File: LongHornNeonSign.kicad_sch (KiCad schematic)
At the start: 19 parts, among them Q1 IRLZ44N, Q2 IRLZ44N, Q3 IRLZ44N

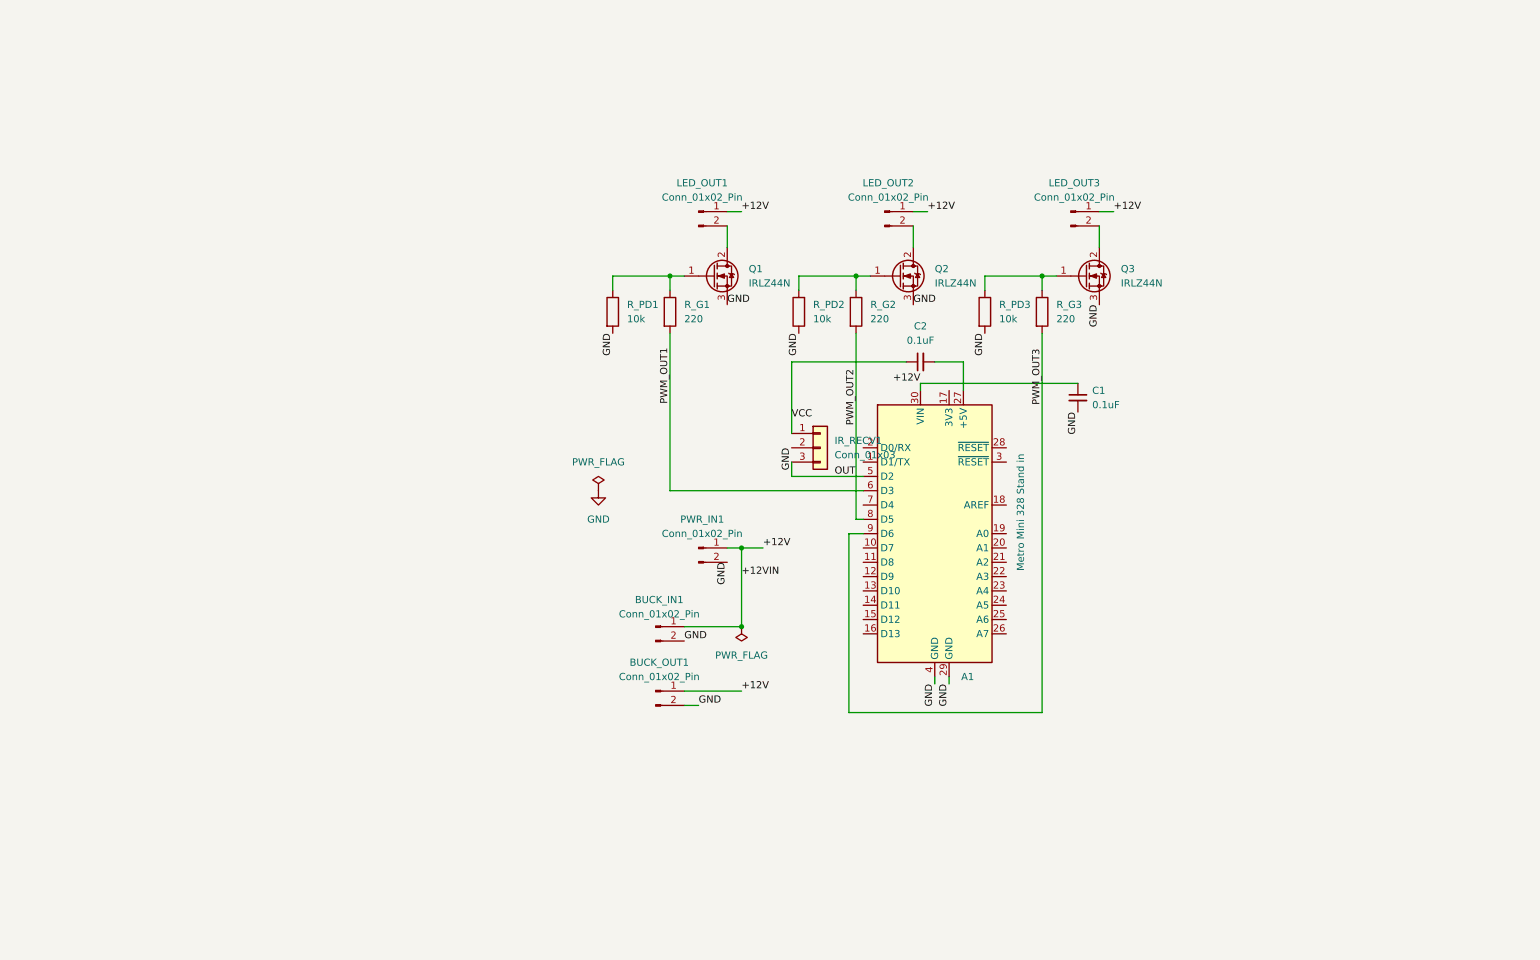
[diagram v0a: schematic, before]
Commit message: Fixed schematic
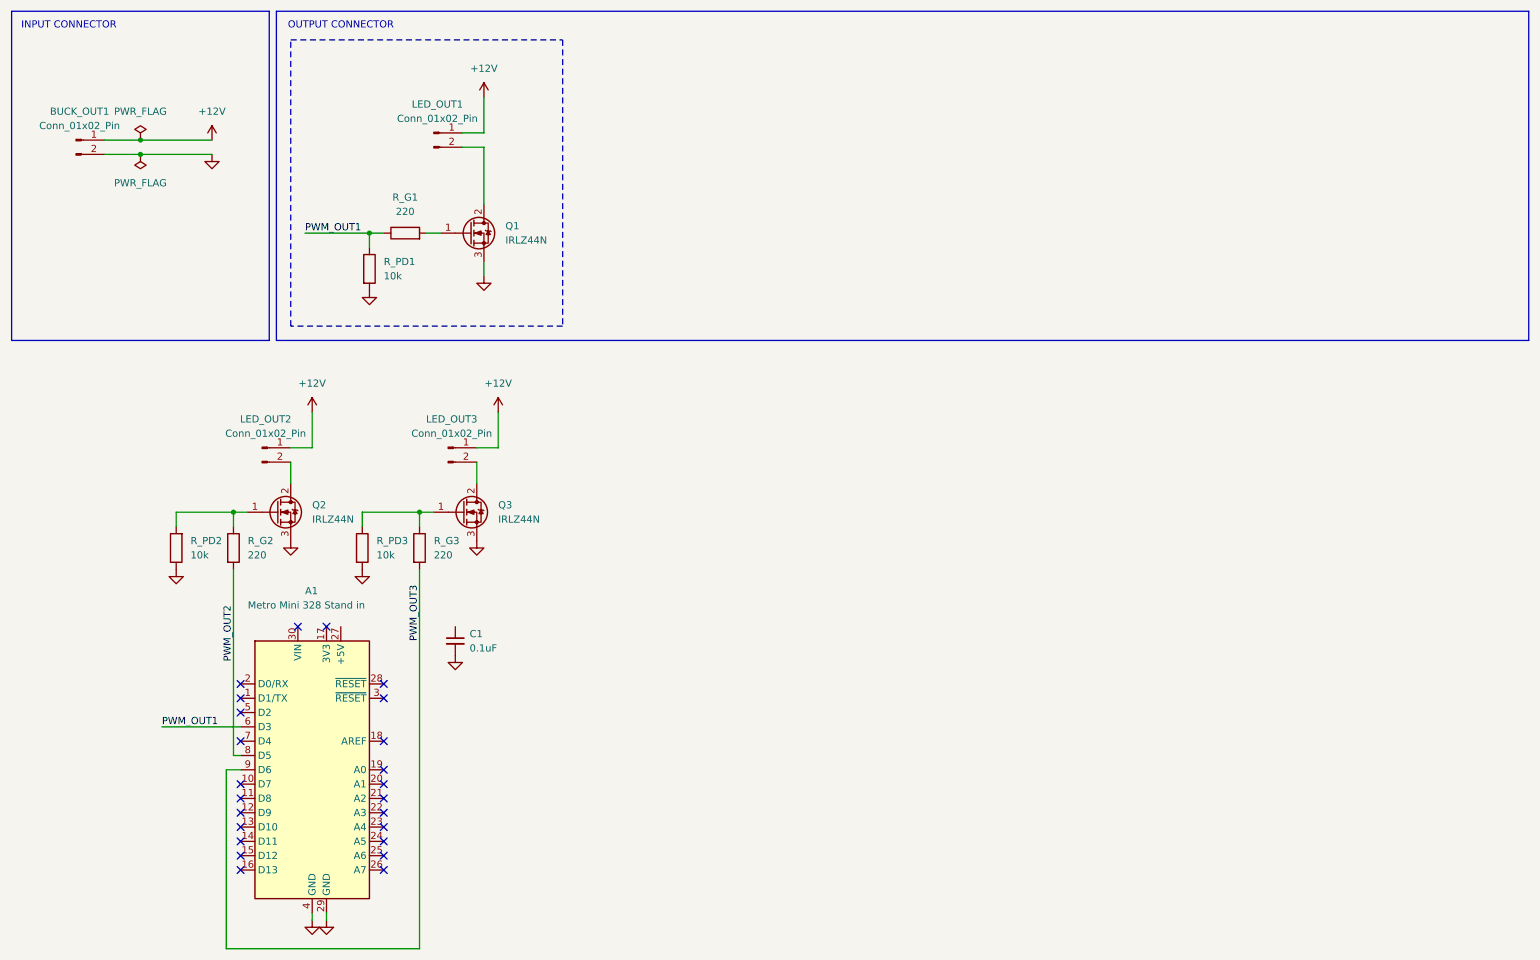
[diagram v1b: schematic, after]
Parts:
- removed BUCK_IN1, PWR_IN1: Conn_01x02_Pin, Connector_PinHeader_2.54mm:PinHeader_1x02_P2.54mm_Vertical, symbol Connector:Conn_01x02_Pin
- removed C2: 0.1uF, Capacitor_SMD:C_0805_2012Metric, symbol Device:C_Small
- removed IR_RECV1: Conn_01x03, Connector_PinHeader_2.54mm:PinHeader_1x03_P2.54mm_Vertical, symbol Connector_Generic:Conn_01x03
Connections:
- net PWM_OUT1: now also R_G1.1, R_PD1.1; no longer R_G1.2
- net +12V  renamed +12V
- net +12V: no longer A1.30 (VIN), C1.1
- net OUT: no longer names the net of A1.5 (D2)
- new net: Q1.1 (G), R_G1.2
- no-connect marks 0 -> 24
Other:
- note added: "INPUT CONNECTOR"
- note added: "OUTPUT CONNECTOR"
- moved on the sheet: A1, BUCK_OUT1, C1, LED_OUT1, LED_OUT2, LED_OUT3, Q1, Q2, Q3, R_G1, R_G2, R_G3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

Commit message: update sch
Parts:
- added BUCK_IN1, BUCK_OUT1: Conn_01x02_Pin, Connector_PinHeader_2.54mm:PinHeader_1x02_P2.54mm_Vertical, symbol Connector:Conn_01x02_Pin
- added C_DEBOUNCE1, C_DEBOUNCE2, C_DEBOUNCE3: 0.1uF, Capacitor_SMD:C_0805_2012Metric, symbol Device:C_Small
- added LED_12V1, LED_5V1: LED, LED_THT:LED_D5.0mm, symbol Device:LED
- added LED_OUT4: Conn_01x02_Pin, LED_THT:LED_D5.0mm, symbol Connector:Conn_01x02_Pin
- added Q4: IRLZ44N, Package_TO_SOT_THT:TO-220-3_Vertical, symbol Transistor_FET:IRLZ44N
- added R1: 1kΩ, Resistor_THT:R_Axial_DIN0207_L6.3mm_D2.5mm_P7.62mm, symbol Device:R
- added R2: 470Ω, Resistor_THT:R_Axial_DIN0207_L6.3mm_D2.5mm_P7.62mm, symbol Device:R
- added R_G4: 220, Resistor_THT:R_Axial_DIN0207_L6.3mm_D2.5mm_P7.62mm_Horizontal, symbol Device:R
- added R_PD4, R_PD5, R_PD6, R_PD7: 10kΩ, Resistor_THT:R_Axial_DIN0207_L6.3mm_D2.5mm_P7.62mm_Horizontal, symbol Device:R
- added SW1, SW2, SW3: SW_Push, Button_Switch_THT:SW_PUSH_6mm, symbol Switch:SW_Push
- A1: value Metro Mini 328 Stand in -> Arduino Nano
- R_PD1, R_PD2, R_PD3: value 10k -> 10kΩ
- renumbered BUCK_OUT1 to PWR_IN1
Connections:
- net +12V: now also BUCK_IN1.1 (Pin_1), LED_OUT4.1 (Pin_1), R1.1
- net GND: now also R_PD2.2, BUCK_IN1.2 (Pin_2), BUCK_OUT1.2 (Pin_2), C_DEBOUNCE1.1, C_DEBOUNCE2.1, C_DEBOUNCE3.1, LED_12V1.2 (A), LED_5V1.2 (A), Q4.3 (S), R_PD4.2, R_PD5.2, R_PD6.2, R_PD7.2; no longer R_PD2.1
- net PWM_OUT2: now also R_G2.1, R_PD2.1; no longer R_G2.2
- net PWM_OUT3: now also R_G3.1, R_PD3.1; no longer R_G3.2
- net at C1.1: now also A1.27 (+5V)
- net BTN_DOWN: now reaches A1.10 (D7)
- net BTN_DOWN: now also C_DEBOUNCE3.2, R_PD6.1, SW3.2
- net PWM_OUT4: now reaches A1.11 (D8)
- net PWM_OUT4: now also R_G4.1, R_PD7.1
- net BTN_TOGGLE: now reaches A1.5 (D2)
- net BTN_TOGGLE: now also C_DEBOUNCE1.2, R_PD4.1, SW1.2
- net BTN_UP: now reaches A1.7 (D4)
- net BTN_UP: now also C_DEBOUNCE2.2, R_PD5.1, SW2.2
- new net: LED_5V1.1 (K), R2.2
- new net: LED_OUT4.2 (Pin_2), Q4.2 (D)
- new net: Q3.1 (G), R_G3.2
- new net: LED_12V1.1 (K), R1.2
- new net: Q4.1 (G), R_G4.2
- new net: Q2.1 (G), R_G2.2
- new net +5V: BUCK_OUT1.1 (Pin_1), R2.1, SW1.1, SW2.1, SW3.1
- no-connect marks 24 -> 20
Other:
- note added: "BUCK CONVERTER"
- note added: "BUTTONS"
- note added: "DEBUG LEDS"
- note added: "OUTPUT CONNECTOR (1)"
- note added: "OUTPUT CONNECTOR (2)"
- moved on the sheet: A1, C1, LED_OUT1, PWR_IN1, Q1, R_G1, R_PD1

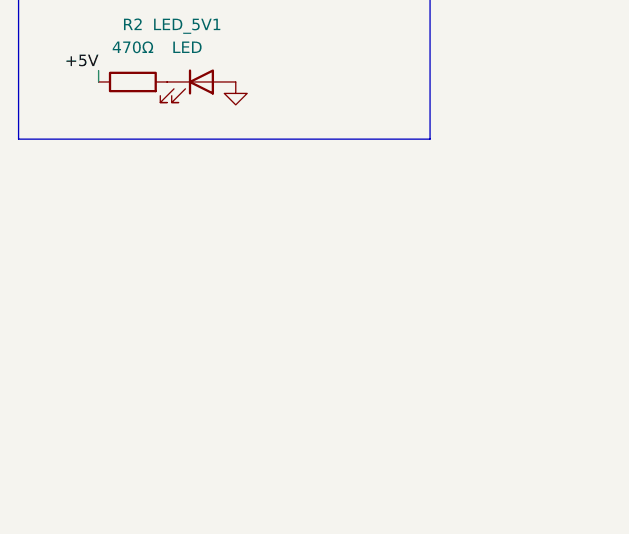
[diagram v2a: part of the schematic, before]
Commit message: Added testpoint example
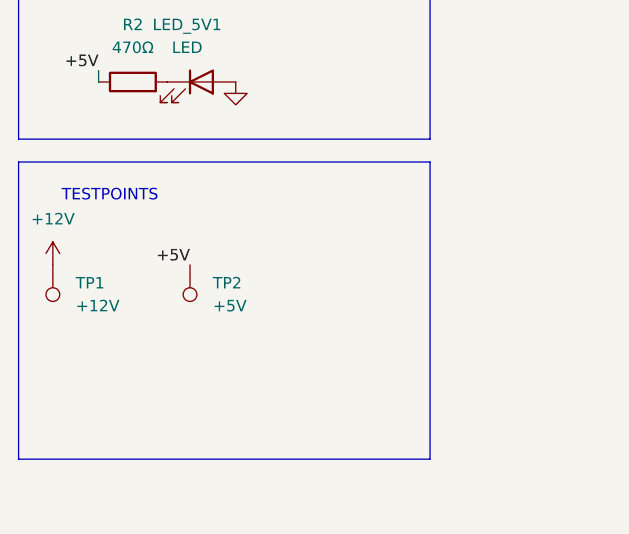
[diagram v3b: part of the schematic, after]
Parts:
- added TP1: +12V, Connector_PinHeader_2.54mm:PinHeader_1x01_P2.54mm_Vertical, symbol Connector:TestPoint
- added TP2: +5V, Connector_PinHeader_2.54mm:PinHeader_1x01_P2.54mm_Vertical, symbol Connector:TestPoint
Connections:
- net +12V: now also TP1.1
- net +5V: now also TP2.1
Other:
- note added: "TESTPOINTS"
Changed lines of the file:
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@@
+	)
+	(rectangle
+		(start 13.97 110.49)
+		(end 59.69 143.51)
+		(stroke
+			(width 0)
+			(type default)
+		)
+		(fill
+			(type none)
+		)
 	)
 	(rectangle
@@
 		(fill
 			(type none)
+		)
+	)
+	(text "TESTPOINTS\n"
+		(exclude_from_sim no)
+		(at 24.13 114.3 0)
+		(effects
+			(font
+				(size 1.27 1.27)
+			)
 		)
 	)
@@
 	(label "BTN_TOGGLE"
 		(at 100.33 110.49 180)
+		(effects
+			(font
+				(size 1.27 1.27)
+			)
+			(justify right bottom)
+		)
+	)
+	(label "+5V"
+		(at 33.02 121.92 180)
 		(effects
 			(font
@@
 	)
 	(symbol
+		(lib_id "Connector:TestPoint")
+		(at 33.02 121.92 180)
+		(unit 1)
+		(exclude_from_sim no)
+		(in_bom yes)
+		(on_board yes)
+		(dnp no)
+		(fields_autoplaced yes)
+		(property "Reference" "TP2"
+			(at 35.56 123.9519 0)
+			(effects
+				(font
+					(size 1.27 1.27)
+				)
+				(justify right)
+			)
+		)
+		(property "Value" "+5V"
+			(at 35.56 126.4919 0)
+			(effects
+				(font
+					(size 1.27 1.27)
+				)
+				(justify right)
+			)
+		)
+		(property "Footprint" "Connector_PinHeader_2.54mm:PinHeader_1x01_P2.54mm_Vertical"
+			(at 27.94 121.92 0)
+			(effects
+				(font
+					(size 1.27 1.27)
+				)
+				(hide yes)
+			)
+		)
+		(property "Datasheet" "~"
+			(at 27.94 121.92 0)
+			(effects
+				(font
+					(size 1.27 1.27)
+				)
+				(hide yes)
+			)
+		)
+		(property "Description" "test point"
+			(at 33.02 121.92 0)
+			(effects
+				(font
+					(size 1.27 1.27)
+				)
+				(hide yes)
+			)
+		)
+		(pin "1"
+		)
+		(instances
+			(project "LongHornNeonSign"
+				(path "/f5140a03-2151-4444-9841-b9751d5275da"
+					(reference "TP2")
+					(unit 1)
+				)
+			)
+		)
+	)
+	(symbol
 		(lib_id "power:GND")
 		(at 101.6 60.96 0)
@@
 	)
 	(symbol
+		(lib_id "power:+12V")
+		(at 17.78 121.92 0)
+		(unit 1)
+		(exclude_from_sim no)
+		(in_bom yes)
+		(on_board yes)
+		(dnp no)
+		(fields_autoplaced yes)
+		(property "Reference" "#PWR030"
+			(at 17.78 125.73 0)
+			(effects
+				(font
+					(size 1.27 1.27)
+				)
+				(hide yes)
+			)
+		)
+		(property "Value" "+12V"
+			(at 17.78 116.84 0)
+			(effects
+				(font
+					(size 1.27 1.27)
+				)
+			)
+		)
+		(property "Footprint" ""
+			(at 17.78 121.92 0)
+			(effects
+				(font
+					(size 1.27 1.27)
+				)
+				(hide yes)
+			)
+		)
+		(property "Datasheet" ""
+			(at 17.78 121.92 0)
+			(effects
+				(font
+					(size 1.27 1.27)
+				)
+				(hide yes)
+			)
+		)
+		(property "Description" "Power symbol creates a global label with name \"+12V\""
+			(at 17.78 121.92 0)
+			(effects
+				(font
+					(size 1.27 1.27)
+				)
+				(hide yes)
+			)
+		)
+		(pin "1"
+		)
+		(instances
+			(project "LongHornNeonSign"
+				(path "/f5140a03-2151-4444-9841-b9751d5275da"
+					(reference "#PWR030")
+					(unit 1)
+				)
+			)
+		)
+	)
+	(symbol
 		(lib_id "Device:C_Small")
 		(at 128.27 96.52 0)
@@
 					(unit 1)
 				)
+			)
+		)
+	)
+	(symbol
+		(lib_id "Connector:TestPoint")
+		(at 17.78 121.92 180)
+		(unit 1)
+		(exclude_from_sim no)
+		(in_bom yes)
+		(on_board yes)
+		(dnp no)
+		(fields_autoplaced yes)
+		(property "Reference" "TP1"
+			(at 20.32 123.9519 0)
+			(effects
+				(font
+					(size 1.27 1.27)
+				)
+				(justify right)
+			)
+		)
+		(property "Value" "+12V"
+			(at 20.32 126.4919 0)
+			(effects
+				(font
+					(size 1.27 1.27)
+				)
+				(justify right)
+			)
+		)
+		(property "Footprint" "Connector_PinHeader_2.54mm:PinHeader_1x01_P2.54mm_Vertical"
+			(at 12.7 121.92 0)
+			(effects
+				(font
+					(size 1.27 1.27)
+				)
+				(hide yes)
+			)
+		)
+		(property "Datasheet" "~"
+			(at 12.7 121.92 0)
+			(effects
+				(font
+					(size 1.27 1.27)
+				)
+				(hide yes)
+			)
+		)
+		(property "Description" "test point"
+			(at 17.78 121.92 0)
+			(effects
+				(font
+					(size 1.27 1.27)
+				)
+				(hide yes)
+			)
+		)
+		(pin "1"
+		)
+		(instances
+			(project ""
+				(path "/f5140a03-2151-4444-9841-b9751d5275da"
+					(reference "TP1")
+					(unit 1)
+				)

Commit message: update
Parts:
- removed BUCK_IN1, BUCK_OUT1: Conn_01x02_Pin, Connector_PinHeader_2.54mm:PinHeader_1x02_P2.54mm_Vertical, symbol Connector:Conn_01x02_Pin
- added C2: C_Small, Capacitor_SMD:C_0805_2012Metric, symbol Device:C_Small
- added CIN1: 680μF, symbol Device:C_Polarized
- added COUT1: 220μF, symbol Device:C_Polarized
- added D1: 1N5822, Diode_THT:D_DO-201AD_P15.24mm_Horizontal, symbol Diode:1N5822
- added L1: 33μH, symbol Device:L
- added LED_5V2, LED_5V3, LED_5V4, LED_5V5, LED_5V6, LED_5V7, LED_5V8: LED, LED_THT:LED_D5.0mm, symbol Device:LED
- added R3, R4, R5, R6, R7, R8, R9: 470Ω, Resistor_THT:R_Axial_DIN0207_L6.3mm_D2.5mm_P7.62mm, symbol Device:R
- added TP3, TP4, TP5, TP6, TP7, TP8, TP9: +5V, Connector_PinHeader_2.54mm:PinHeader_1x01_P2.54mm_Vertical, symbol Connector:TestPoint
- added U1: LM2596S-5, Package_TO_SOT_SMD:TO-263-5_TabPin3, symbol Regulator_Switching:LM2596S-5
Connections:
- net +12V: now also CIN1.1, U1.1 (VIN)
- net +5V: now also COUT1.1, L1.2, U1.4 (FB)
- net BTN_DOWN: now also TP4.1
- net BTN_TOGGLE: now also TP3.1
- net BTN_UP: now also TP5.1
- net GND: now also C2.2, CIN1.2, COUT1.2, D1.2 (A), LED_5V2.2 (A), LED_5V3.2 (A), LED_5V4.2 (A), LED_5V5.2 (A), LED_5V6.2 (A), LED_5V7.2 (A), LED_5V8.2 (A), U1.3 (GND), U1.5 (~{ON}/OFF)
- net PWM_OUT1: now also TP8.1
- net PWM_OUT2: now also TP7.1
- net PWM_OUT3: now also TP6.1
- net PWM_OUT4: now also TP9.1
- net D_DEBUG1: now reaches A1.1 (D1/TX)
- net D_DEBUG1: now also R4.1
- net D_DEBUG9: now reaches A1.12 (D9)
- net D_DEBUG9: now also R5.1
- net D_DEBUG10: now reaches A1.13 (D10)
- net D_DEBUG10: now also R6.1
- net D_DEBUG11: now reaches A1.14 (D11)
- net D_DEBUG11: now also R7.1
- net D_DEBUG12: now reaches A1.15 (D12)
- net D_DEBUG12: now also R8.1
- net D_DEBUG13: now reaches A1.16 (D13)
- net D_DEBUG13: now also R9.1
- net D_DEBUG0: now reaches A1.2 (D0/RX)
- net D_DEBUG0: now also R3.1
- new net: LED_5V6.1 (K), R7.2
- new net: D1.1 (K), L1.1, U1.2 (OUT)
- new net: LED_5V7.1 (K), R8.2
- new net: LED_5V3.1 (K), R4.2
- new net: LED_5V8.1 (K), R9.2
- new net: LED_5V2.1 (K), R3.2
- new net: LED_5V5.1 (K), R6.2
- new net: LED_5V4.1 (K), R5.2
- no-connect marks 20 -> 14
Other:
- moved on the sheet: LED_12V1, LED_5V1, R1, R2, TP2

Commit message: new
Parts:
- TP3: value +5V -> BTN_TOGGLE
- TP4: value +5V -> BTN_DOWN
- TP5: value +5V -> BTN_UP
- TP6: value +5V -> PWM_OUT3
- TP7: value +5V -> PWM_OUT2
- TP8: value +5V -> PWM_OUT1
- TP9: value +5V -> PWM_OUT4
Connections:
- net +5V: now also A1.27 (+5V), C1.1, C2.1
- no-connect marks 14 -> 13
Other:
- moved on the sheet: A1, C1, C2, CIN1, COUT1, D1, L1, TP4, TP5, TP7, TP8, TP9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

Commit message: sch
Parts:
- removed C2: C_Small, Capacitor_SMD:C_0805_2012Metric, symbol Device:C_Small
- removed D1: 1N5822, Diode_THT:D_DO-201AD_P15.24mm_Horizontal, symbol Diode:1N5822
- removed PWR_IN1: Conn_01x02_Pin, Connector_PinHeader_2.54mm:PinHeader_1x02_P2.54mm_Vertical, symbol Connector:Conn_01x02_Pin
- removed Q1, Q2, Q3, Q4: IRLZ44N, Package_TO_SOT_THT:TO-220-3_Vertical, symbol Transistor_FET:IRLZ44N
- added D2: SS34, Diode_SMD:D_SMA, symbol Diode:SS34
- added J1: Barrel_Jack, Connector_BarrelJack:BarrelJack_CUI_PJ-102AH_Horizontal, symbol Connector:Barrel_Jack
- added Q1, Q2, Q3, Q4: AO3400A, Package_TO_SOT_SMD:SOT-23, symbol Transistor_FET:AO3400A
- C1, C_DEBOUNCE1, C_DEBOUNCE2, C_DEBOUNCE3: footprint Capacitor_SMD:C_0805_2012Metric -> Capacitor_SMD:C_0603_1608Metric
- CIN1: footprint (none) -> Capacitor_SMD:CP_Elec_10x10; LCSC (none) -> C47118
- COUT1: footprint (none) -> Capacitor_SMD:CP_Elec_8x10
- L1: footprint (none) -> Inductor_SMD:L_12x12mm_H8mm
- LED_12V1, LED_5V1, LED_5V2, LED_5V3, LED_5V4, LED_5V5, LED_5V6, LED_5V7, LED_5V8: footprint LED_THT:LED_D5.0mm -> LED_SMD:LED_0805_2012Metric
- LED_OUT1, LED_OUT2, LED_OUT3, LED_OUT4: footprint LED_THT:LED_D5.0mm -> TerminalBlock:TerminalBlock_MaiXu_MX126-5.0-02P_1x02_P5.00mm
- R1, R2, R3, R4, R5, R6, R7, R8, R9: footprint Resistor_THT:R_Axial_DIN0207_L6.3mm_D2.5mm_P7.62mm -> Resistor_SMD:R_0805_2012Metric
- R_G1, R_G2, R_G3, R_G4, R_PD1, R_PD2, R_PD3, R_PD4, R_PD5, R_PD6, R_PD7: footprint Resistor_THT:R_Axial_DIN0207_L6.3mm_D2.5mm_P7.62mm_Horizontal -> Resistor_SMD:R_0805_2012Metric
- SW1, SW2, SW3: footprint Button_Switch_THT:SW_PUSH_6mm -> Button_Switch_SMD:SW_Tactile_SPST_NO_Straight_CK_PTS636Sx25SMTRLFS
- U1: LCSC (none) -> C116713
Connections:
- net +12V: now also J1.1
- net GND: now also D2.2 (A), J1.2, Q1.2 (S), Q2.2 (S), Q3.2 (S), Q4.2 (S)
- net at LED_OUT4.2 (Pin_2): now also Q4.3 (D)
- net at LED_OUT3.2 (Pin_2): now also Q3.3 (D)
- net at L1.1, U1.2 (OUT): now also D2.1 (K)
- net at R_G3.2: now also Q3.1 (G)
- net at R_G4.2: now also Q4.1 (G)
- net at R_G1.2: now also Q1.1 (G)
- net at LED_OUT1.2 (Pin_2): now also Q1.3 (D)
- net at R_G2.2: now also Q2.1 (G)
- net at LED_OUT2.2 (Pin_2): now also Q2.3 (D)

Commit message: sch done
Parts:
- removed LED_OUT1, LED_OUT2, LED_OUT3, LED_OUT4: Conn_01x02_Pin, TerminalBlock:TerminalBlock_MaiXu_MX126-5.0-02P_1x02_P5.00mm, symbol Connector:Conn_01x02_Pin
- added J2, J3, J4, J5: Screw_Terminal_01x02, TerminalBlock:TerminalBlock_MaiXu_MX126-5.0-02P_1x02_P5.00mm, symbol Connector:Screw_Terminal_01x02
- CIN1: LCSC C47118 -> C2902805
- COUT1: LCSC (none) -> C976031
- C_DEBOUNCE1, C_DEBOUNCE2, C_DEBOUNCE3: LCSC (none) -> C14663
- C_DECOUP: renamed from C1; LCSC (none) -> C14663
- D2: LCSC (none) -> C8678
- J1: LCSC (none) -> C381116
- L1: LCSC (none) -> C2929502
- LED_12V1: value LED -> DL_12V; LCSC (none) -> C375456
- LED_5V1: value LED -> DL_5V; LCSC (none) -> C375456
- LED_5V2: value LED -> DL_D0; LCSC (none) -> C375456
- LED_5V3: value LED -> DL_D1; LCSC (none) -> C375456
- LED_5V4: value LED -> DL_D9; LCSC (none) -> C375456
- LED_5V5: value LED -> DL_D10; LCSC (none) -> C375456
- LED_5V6: value LED -> DL_D11; LCSC (none) -> C375456
- LED_5V7: value LED -> DL_D12; LCSC (none) -> C375456
- LED_5V8: value LED -> DL_D13; LCSC (none) -> C375456
- Q1, Q2, Q3, Q4: LCSC (none) -> C20917
- R1: LCSC (none) -> C95781
- R2, R3, R4, R5, R6, R7, R8, R9: LCSC (none) -> C114564
- R_G1, R_G2, R_G3, R_G4: LCSC (none) -> C104105
- R_PD1, R_PD2, R_PD3, R_PD4, R_PD5, R_PD6, R_PD7: LCSC (none) -> C17414
- SW1, SW2, SW3: LCSC (none) -> C10852
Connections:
- net +12V: now also J2.2 (Pin_2), J3.2 (Pin_2), J4.2 (Pin_2), J5.2 (Pin_2)
- net at Q4.3 (D): now also J5.1 (Pin_1)
- net at Q3.3 (D): now also J4.1 (Pin_1)
- net at Q1.3 (D): now also J2.1 (Pin_1)
- net at Q2.3 (D): now also J3.1 (Pin_1)

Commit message: update
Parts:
- added TPGND1: GND, Connector_PinHeader_2.54mm:PinHeader_1x01_P2.54mm_Vertical, symbol Connector:TestPoint
- J2, J3, J4, J5: footprint TerminalBlock:TerminalBlock_MaiXu_MX126-5.0-02P_1x02_P5.00mm -> TerminalBlock_Phoenix:TerminalBlock_Phoenix_MKDS-1,5-2-5.08_1x02_P5.08mm_Horizontal; LCSC C395885 -> C8465
- renumbered C_DECOUP to C_DECOUP1, TP1 to TP12V1, TP2 to TP5V1, TP4 to TP_DOWN1, TP8 to TP_PWM1, TP7 to TP_PWM2, TP6 to TP_PWM3, TP9 to TP_PWM4, TP3 to TP_TOG1, TP5 to TP_UP1
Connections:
- net D_DEBUG10: now also A1.20 (A1); no longer A1.13 (D10)
- net D_DEBUG11: now also A1.21 (A2); no longer A1.14 (D11)
- net D_DEBUG12: now also A1.22 (A3); no longer A1.15 (D12)
- net D_DEBUG9: now also A1.19 (A0); no longer A1.12 (D9)
- net GND: now also TPGND1.1
